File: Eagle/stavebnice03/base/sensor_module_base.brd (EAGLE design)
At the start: 5 parts

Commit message: I did an order in Eagle files
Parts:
- added C1, C3, C4, C5: 100nF, resistor:C0603
- added R1, R2, R4: 2k2, resistor:R0603
- added R3: 2K2, resistor:R0603
- added U$2, U$3, U$6, U$7: NC7SB3157P6X, !stavebnice03:SC70-6L
- added U$5: JUMPER5F-90, !stavebnice03:JUMPER5F-90
- moved C2 2.56 mm to (7.30, 12.2), turned to 90 degrees
- moved U$9 0.20 mm to (5.50, 1.55)
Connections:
- new net N$1: U$1.3, U$6.6, U$7.6
- new net N$10: R2.1, U$5.2, U$6.3, U$7.1
- new net N$20: U$2.3, U$7.4
- new net N$4: U$1.9, U$3.4
- new net N$6: R1.1, U$5.4, U$6.1, U$7.3
- new net N$7: U$3.3, U$6.4
- new net N$8: R4.1, U$3.1, U$4.2
- new net N$9: U$1.2, U$2.6, U$3.6
- net GND: now also C1.2, C3.1, C4.2, C5.1, U$2.2, U$3.2, U$5.1, U$5.5, U$6.2, U$7.2
- net N$2: now also U$2.4; no longer U$4.2
- net N$5: now also R3.1, U$2.1; no longer U$1.9
- net VCC: now also C1.1, C3.2, C4.1, C5.2, R1.2, R2.2, R3.2, R4.2, U$2.5, U$3.5, U$5.3, U$6.5, U$7.5; no longer U$1.2, U$1.3
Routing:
- net GND: track 22.0 -> 82.5 mm, vias 0 -> 2
- net N$4: track 0.00 -> 27.3 mm, vias 0 -> 2
- net N$1: track 0.00 -> 25.2 mm
- net N$9: track 0.00 -> 20.9 mm, vias 0 -> 2
- net VCC: track 33.7 -> 51.7 mm, vias 0 -> 3
- net N$20: track 0.00 -> 17.7 mm, vias 0 -> 2
- net N$13: track 32.0 -> 21.4 mm
- net N$6: track 0.00 -> 10.1 mm, vias 0 -> 1
- net N$10: track 0.00 -> 9.27 mm, vias 0 -> 1
- net N$8: track 0.00 -> 8.23 mm
- net N$2: track 15.8 -> 9.30 mm, vias 0 -> 2
- net N$7: track 0.00 -> 3.13 mm
- net N$14: track 8.56 -> 10.9 mm
- net N$5: track 10.0 -> 11.4 mm, vias 0 -> 1
- net N$12: track 11.8 -> 13.0 mm
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- added copper zone on layer 16, net N$2
- added copper zone on layer 1, net N$20
- added copper zone on layer 16, net N$20
- added copper zone on layer 1, net N$4
- removed copper zone on layer 16, net N$3

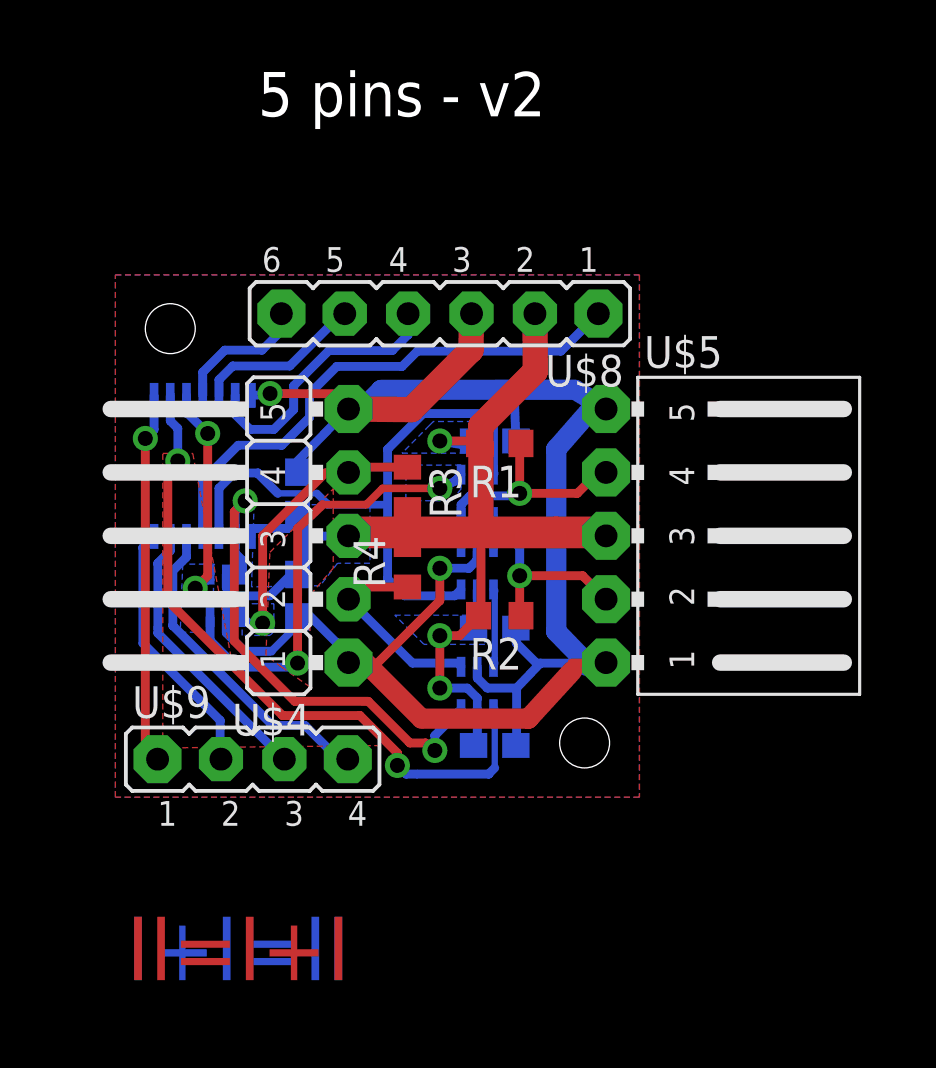
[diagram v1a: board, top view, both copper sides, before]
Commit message: added wire from input bus to an iterrupt pin
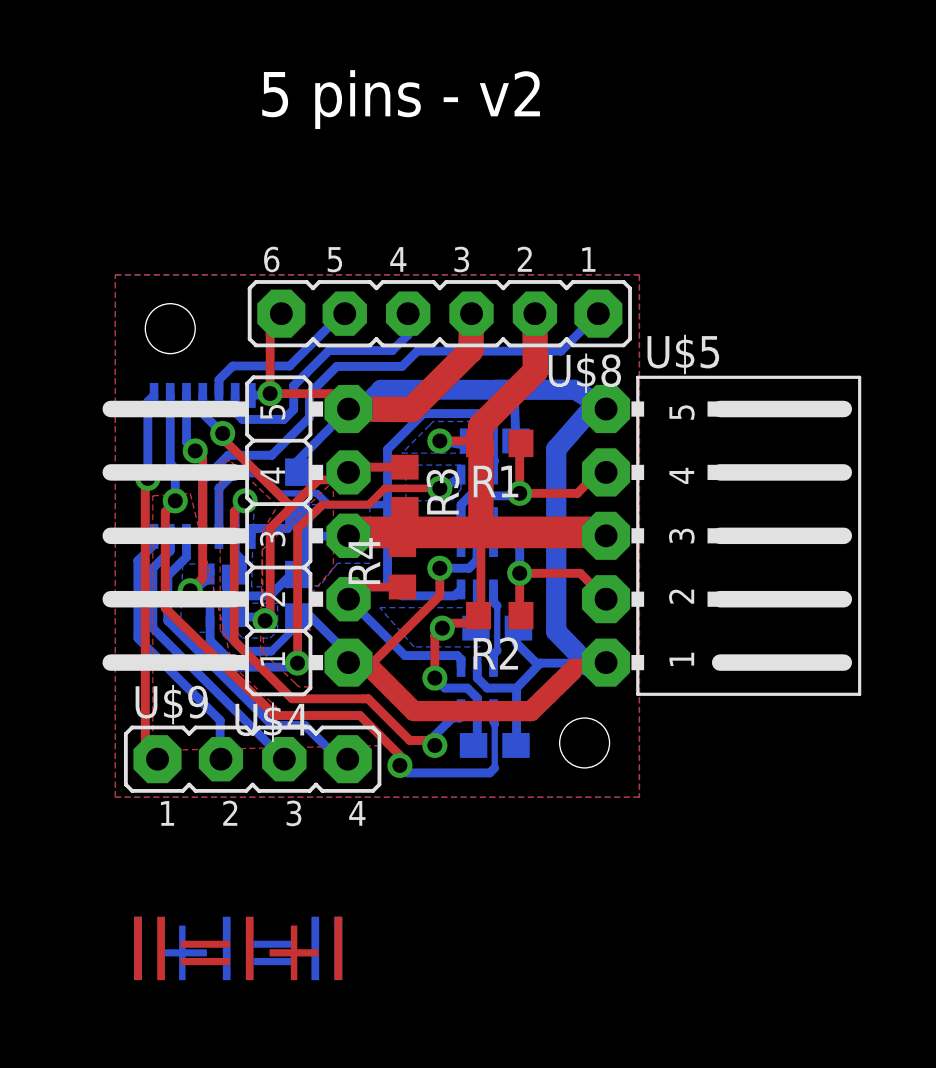
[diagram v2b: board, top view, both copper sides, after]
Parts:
- moved R4 0.20 mm to (11.5, 9.30)
- moved C3 0.10 mm to (15.3, 6.80)
- moved R3 0.10 mm to (11.6, 12.4)
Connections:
- removed net N$5: R3.1, U$2.1, U$4.4
- net GND: now also U$8.6
- net N$11: now also R3.1, U$2.1, U$4.4; no longer U$8.6
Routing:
- net N$11: track 5.46 -> 17.1 mm, vias 0 -> 2
- net N$5: track 11.4 -> 0.00 mm, vias 1 -> 0
- net GND: track 82.5 -> 85.4 mm
- net VCC: track 51.7 -> 52.3 mm
- added copper zone on layer 16, net N$11
- added copper zone on layer 1, net N$9
- removed copper zone on layer 16, net N$5

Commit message: base and battery module size increeased to 22x22
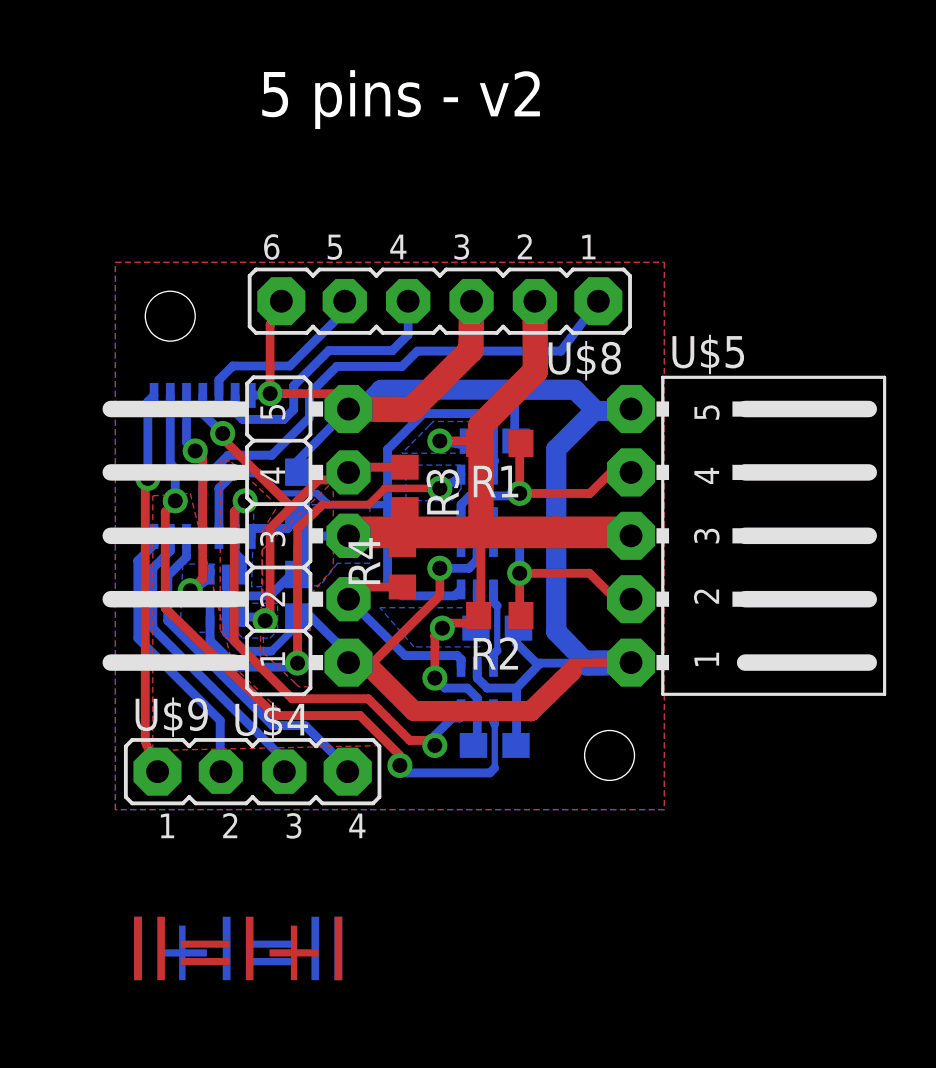
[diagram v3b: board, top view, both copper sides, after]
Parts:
- moved U$5 1.00 mm to (23.2, 10.5)
- moved U$8 0.50 mm to (13.0, 19.9)
- moved U$9 0.50 mm to (5.50, 1.05)
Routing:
- net GND: track 85.4 -> 88.7 mm
- net N$10: track 9.31 -> 10.3 mm
- net N$6: track 10.1 -> 11.1 mm
- net VCC: track 52.3 -> 53.2 mm
- net N$14: track 10.5 -> 11.0 mm

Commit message: added pin and resistor to stay in bootloader + changed size back to 21x21 mm
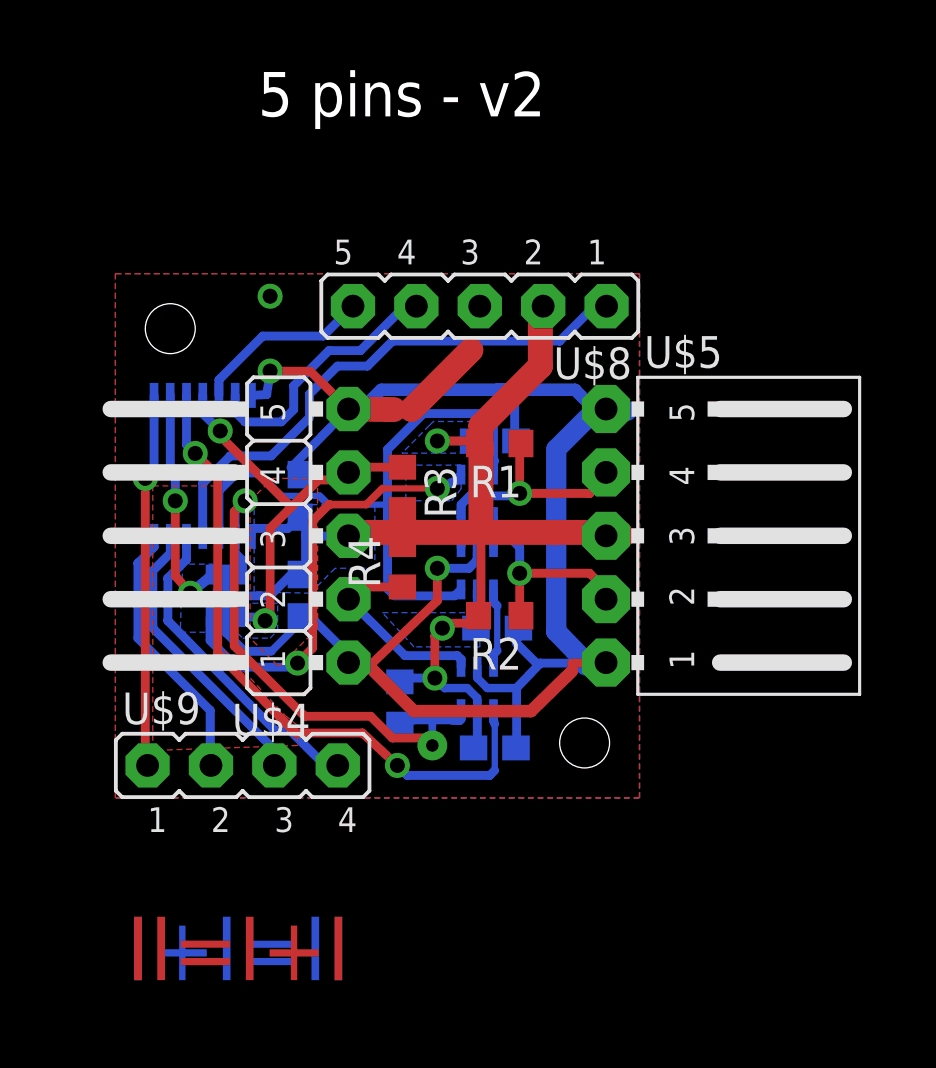
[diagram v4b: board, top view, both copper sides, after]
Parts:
- added R5: 100k, resistor:R0603
- U$8: value JUMPER6M -> JUMPER5M; device !stavebnice03:JUMPER6M -> !stavebnice03:JUMPER5M
- moved U$8 1.61 mm to (14.6, 19.7)
- moved U$5 1.00 mm to (22.2, 10.5)
- moved U$9 0.47 mm to (5.10, 1.30)
- moved C2 0.14 mm to (7.40, 12.1)
- moved C1 0.10 mm to (7.40, 8.10)
- moved C4 0.10 mm to (15.2, 2.00)
- moved R3 0.10 mm to (11.5, 12.4)
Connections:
- net GND: no longer U$8.6
- net N$2: now also U$1.9; no longer U$1.10
- net N$4: now also U$1.10; no longer U$1.9
- net N$9: now also R5.1
- net VCC: now also R5.2
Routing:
- net GND: track 88.7 -> 82.8 mm, vias 2 -> 3
- net N$9: track 20.9 -> 22.9 mm
- net VCC: track 53.2 -> 55.0 mm
- net N$4: track 27.3 -> 26.5 mm
- net N$12: track 13.5 -> 12.9 mm
- net N$6: track 11.1 -> 10.5 mm
- added copper zone on layer 1, net N$11
- added copper zone on layer 1, net N$2
- removed copper zone on layer 1, net N$20
- removed copper zone on layer 1, net N$4
- removed copper zone on layer 1, net N$9

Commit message: minor element position changes
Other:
- board text added: "sensor base"
- board text removed: "5 pins - v2"
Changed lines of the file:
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@@
 <grid distance="0.1" unitdist="mm" unit="mm" style="lines" multiple="1" display="no" altdistance="0.025" altunitdist="inch" altunit="inch"/>
 <layers>
-<layer number="1" name="Top" color="4" fill="1" visible="yes" active="yes"/>
-<layer number="16" name="Bottom" color="1" fill="1" visible="no" active="yes"/>
+<layer number="1" name="Top" color="4" fill="1" visible="no" active="yes"/>
+<layer number="16" name="Bottom" color="1" fill="1" visible="yes" active="yes"/>
 <layer number="17" name="Pads" color="2" fill="1" visible="yes" active="yes"/>
 <layer number="18" name="Vias" color="2" fill="1" visible="yes" active="yes"/>
 <layer number="19" name="Unrouted" color="6" fill="1" visible="yes" active="yes"/>
 <layer number="20" name="Dimension" color="15" fill="1" visible="yes" active="yes"/>
-<layer number="21" name="tPlace" color="7" fill="1" visible="yes" active="yes"/>
-<layer number="22" name="bPlace" color="7" fill="1" visible="yes" active="yes"/>
-<layer number="23" name="tOrigins" color="15" fill="1" visible="yes" active="yes"/>
-<layer number="24" name="bOrigins" color="15" fill="1" visible="yes" active="yes"/>
+<layer number="21" name="tPlace" color="7" fill="1" visible="no" active="yes"/>
+<layer number="22" name="bPlace" color="7" fill="1" visible="no" active="yes"/>
+<layer number="23" name="tOrigins" color="15" fill="1" visible="no" active="yes"/>
+<layer number="24" name="bOrigins" color="15" fill="1" visible="no" active="yes"/>
 <layer number="25" name="tNames" color="7" fill="1" visible="no" active="yes"/>
 <layer number="26" name="bNames" color="7" fill="1" visible="no" active="yes"/>
@@
 <layer number="43" name="vRestrict" color="2" fill="10" visible="no" active="yes"/>
 <layer number="44" name="Drills" color="7" fill="1" visible="no" active="yes"/>
-<layer number="45" name="Holes" color="7" fill="1" visible="yes" active="yes"/>
+<layer number="45" name="Holes" color="7" fill="1" visible="no" active="yes"/>
 <layer number="46" name="Milling" color="3" fill="1" visible="no" active="yes"/>
 <layer number="47" name="Measures" color="7" fill="1" visible="no" active="yes"/>
@@
 <text x="4.92125" y="-6.0325" size="2.54" layer="16" rot="MR0" align="center">II=I+I</text>
 <text x="4.92125" y="-6.0325" size="2.54" layer="1" align="center">II=I+I</text>
-<text x="5.715" y="27.305" size="1.778" layer="20">5 pins - v2</text>
-<wire x1="-2" y1="-2.5" x2="24" y2="-2.5" width="0.01" layer="49"/>
-<wire x1="24" y1="-2.5" x2="24" y2="23.5" width="0.01" layer="49"/>
-<wire x1="24" y1="23.5" x2="-2" y2="23.5" width="0.01" layer="49"/>
-<wire x1="-2" y1="23.5" x2="-2" y2="-2.5" width="0.01" layer="49"/>
+<text x="10.5" y="27" size="1.778" layer="20" align="center">sensor base</text>
+<wire x1="-10" y1="-10" x2="31" y2="-10" width="0.01" layer="49"/>
+<wire x1="31" y1="-10" x2="31" y2="31" width="0.01" layer="49"/>
+<wire x1="31" y1="31" x2="-10" y2="31" width="0.01" layer="49"/>
+<wire x1="-10" y1="31" x2="-10" y2="-10" width="0.01" layer="49"/>
+<circle x="2.2" y="18.8" radius="0.6" width="0.9" layer="116"/>
+<circle x="18.8" y="2.2" radius="0.6" width="0.9" layer="116"/>
+<circle x="9.34" y="5.42" radius="0.329" width="0.357" layer="116"/>
+<circle x="9.34" y="7.96" radius="0.329" width="0.357" layer="116"/>
+<circle x="9.34" y="10.5" radius="0.329" width="0.357" layer="116"/>
+<circle x="9.34" y="13.04" radius="0.329" width="0.357" layer="116"/>
+<circle x="9.34" y="15.58" radius="0.329" width="0.357" layer="116"/>
+<circle x="19.66" y="5.42" radius="0.329" width="0.357" layer="116"/>
+<circle x="19.66" y="7.96" radius="0.329" width="0.357" layer="116"/>
+<circle x="19.66" y="10.5" radius="0.329" width="0.357" layer="116"/>
+<circle x="19.66" y="13.04" radius="0.329" width="0.357" layer="116"/>
+<circle x="19.66" y="15.58" radius="0.329" width="0.357" layer="116"/>
+<circle x="19.68" y="19.7" radius="0.329" width="0.357" layer="116"/>
+<circle x="17.14" y="19.7" radius="0.329" width="0.357" layer="116"/>
+<circle x="14.6" y="19.7" radius="0.329" width="0.357" layer="116"/>
+<circle x="12.06" y="19.7" radius="0.329" width="0.357" layer="116"/>
+<circle x="9.52" y="19.7" radius="0.329" width="0.357" layer="116"/>
+<circle x="1.29" y="1.3" radius="0.329" width="0.357" layer="116"/>
+<circle x="3.83" y="1.3" radius="0.329" width="0.357" layer="116"/>
+<circle x="6.37" y="1.3" radius="0.329" width="0.357" layer="116"/>
+<circle x="8.91" y="1.3" radius="0.329" width="0.357" layer="116"/>
+<circle x="12.9" y="9.2" radius="0.25" width="0.2" layer="116"/>
+<circle x="6.2" y="17.1" radius="0.25" width="0.2" layer="116"/>
+<circle x="6.2" y="20.1" radius="0.25" width="0.2" layer="116"/>
+<circle x="3" y="8.2" radius="0.25" width="0.2" layer="116"/>
+<circle x="2.4" y="11.9" radius="0.25" width="0.2" layer="116"/>
+<circle x="3.2" y="13.8" radius="0.25" width="0.2" layer="116"/>
+<circle x="11.3" y="1.3" radius="0.25" width="0.2" layer="116"/>
+<circle x="16.2" y="12.2" radius="0.25" width="0.2" layer="116"/>
+<circle x="5.2" y="11.9" radius="0.25" width="0.2" layer="116"/>
+<circle x="12.7" y="2.1" radius="0.225" width="0.15" layer="116"/>
+<circle x="16.2" y="9" radius="0.25" width="0.2" layer="116"/>
+<circle x="4.2" y="14.7" radius="0.25" width="0.2" layer="116"/>
+<circle x="6" y="7.1" radius="0.25" width="0.2" layer="116"/>
+<circle x="1.2" y="12.8" radius="0.25" width="0.2" layer="116"/>
+<circle x="7.3" y="5.4" radius="0.25" width="0.2" layer="116"/>
+<circle x="12.9" y="12.4" radius="0.25" width="0.2" layer="116"/>
+<circle x="12.9" y="14.3" radius="0.25" width="0.2" layer="116"/>
+<circle x="13.1" y="6.8" radius="0.25" width="0.2" layer="116"/>
+<circle x="12.8" y="4.8" radius="0.25" width="0.2" layer="116"/>
 </plain>
 <attributes>
@@
 <contactref element="U$1" pad="5"/>
 <contactref element="U$9" pad="4"/>
-<wire x1="6.4" y1="2.7" x2="2.1" y2="7.1" width="0.357" layer="16"/>
 <wire x1="2.1" y1="7.1" x2="2.1" y2="8.8" width="0.357" layer="16"/>
 <wire x1="2.1" y1="8.8" x2="2.81875" y2="9.51875" width="0.357" layer="16"/>
-<wire x1="6.4" y1="2.7" x2="7" y2="2.7" width="0.357" layer="16"/>
+<wire x1="6.5" y1="2.7" x2="7" y2="2.7" width="0.357" layer="16"/>
 <wire x1="2.85" y1="10.475" x2="2.85" y2="9.55" width="0.3556" layer="16"/>
 <wire x1="2.85" y1="9.55" x2="2.81875" y2="9.51875" width="0.3556" layer="16"/>
 <wire x1="7" y1="2.7" x2="8.31" y2="1.39" width="0.3556" layer="16"/>
 <wire x1="8.31" y1="1.39" x2="8.91" y2="1.3" width="0.3556" layer="16"/>
+<wire x1="2.1" y1="7.1" x2="6.5" y2="2.7" width="0.3556" layer="16"/>
 </signal>
 <signal name="N$9">
